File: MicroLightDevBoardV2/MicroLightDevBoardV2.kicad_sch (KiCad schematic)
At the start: 77 parts, among them J1 Conn_01x05_Socket, J10 Conn_01x02_Socket, J11 Conn_01x05_Socket, J12 Conn_01x02_Socket, J13 Conn_01x04_Socket, J14 Conn_01x04_Socket, J15 Conn_01x05_Socket, J16 Conn_01x01_Socket, J17 Conn_01x04_Socket, J18 Conn_01x02_Socket, J19 Conn_01x02_Socket, J2 Conn_01x05_Socket, J20 Conn_01x03_Socket, J21 Conn_01x03_Socket, J22 Conn_01x02_Socket, J23 Conn_01x02_Socket, J24 Conn_01x02_Socket, J25 Conn_01x02_Socket, J26 Conn_01x01_Socket, J27 Conn_01x06_Socket, J28 Conn_01x04_Socket, J29 Conn_01x04_Socket, J3 Conn_01x05_Socket, J30 Conn_01x04_Socket, J31 Conn_01x04_Socket, J32 Conn_01x04_Socket, J33 Conn_01x04_Socket, J34 Conn_01x04_Socket, J35 Conn_01x04_Socket, J36 Conn_01x04_Socket, J37 Conn_01x04_Socket, J38 Conn_01x04_Socket, J39 Conn_01x04_Socket, J4 Conn_01x05_Socket, J40 Conn_01x04_Socket, J41 Conn_01x04_Socket, J42 Conn_01x04_Socket, J43 Conn_01x04_Socket, J5 Conn_01x02_Socket, J6 Conn_01x02_Socket, J7 TYPE-C-31-M-12, J8 Conn_01x02_Socket, J9 Conn_01x02_Socket, U1 BQ25628RYKR, U2 ATtiny3226-M, U3 S-85S1AB33-I6T1U, U4 B3U-1000P, U5 B3U-1000P, U6 USBLC6-2P6, U7 MC3479

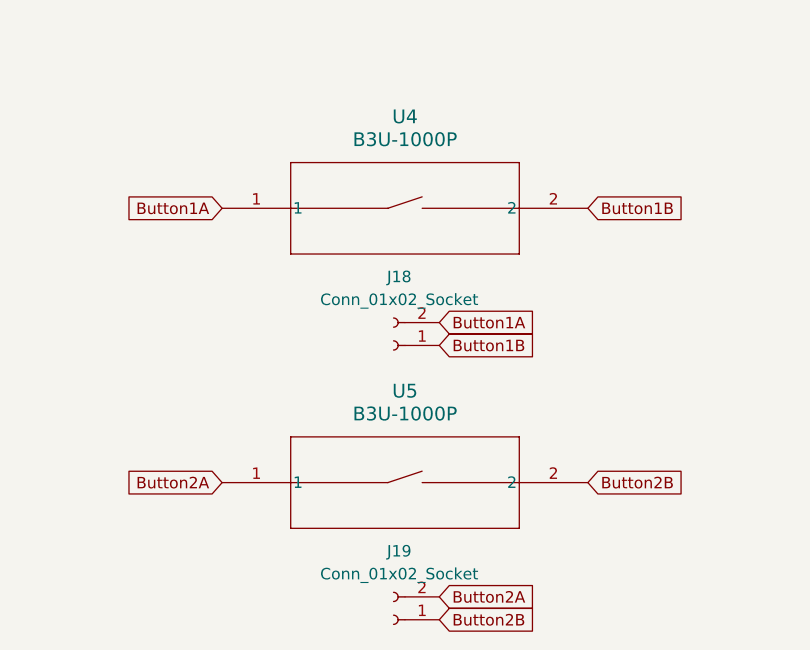
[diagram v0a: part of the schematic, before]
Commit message: add 1uh power inductor footprint from Wurth Elektronik
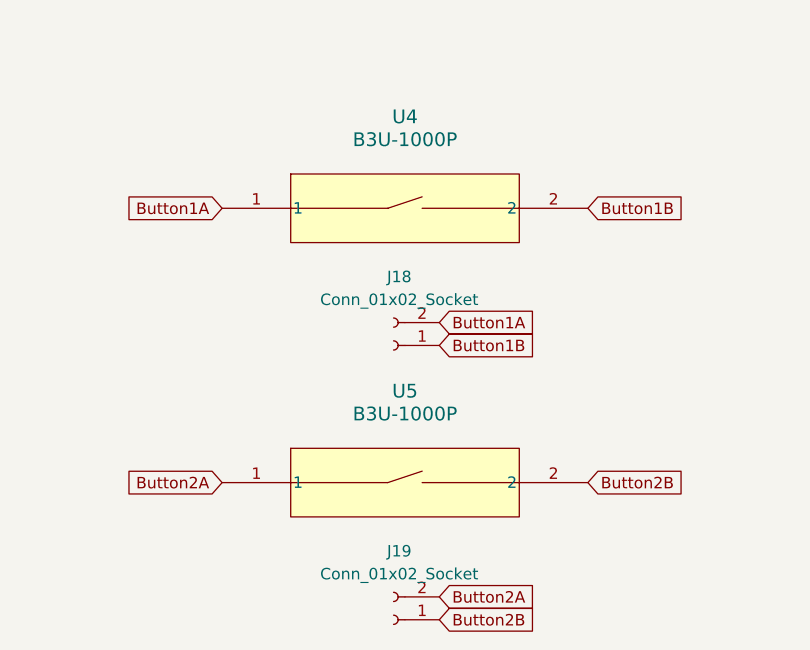
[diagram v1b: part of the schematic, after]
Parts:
- L2: footprint Inductor_SMD:L_0805_2012Metric -> MicroLightDevBoard:IND_2508-WE-MAPI_WRE; purchase (none) -> https://www.mouser.com/ProductDetail/Wurth-Elektronik/74438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
- U4, U5: footprint B3U-1000P -> MicroLightDevBoard:B3U-1000P
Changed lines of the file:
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@@
 			)
 		)
-		(property "Footprint" "Inductor_SMD:L_0805_2012Metric"
+		(property "Footprint" "MicroLightDevBoard:IND_2508-WE-MAPI_WRE"
 			(at 69.85 130.81 0)
 			(effects
@@
 			)
 		)
-		(property "Datasheet" "~"
+		(property "Datasheet" "https://www.we-online.com/components/products/datasheet/74438322010.pdf"
 			(at 69.85 130.81 0)
 			(effects
@@
 			)
 		)
+		(property "purchase" "https://www.mouser.com/ProductDetail/Wurth-Elektronik/74438322010?qs=ZB8tH5z5N7aonmcleKLsGw%3D%3D"
+			(at 69.85 130.81 90)
+			(effects
+				(font
+					(size 1.27 1.27)
+				)
+				(hide yes)
+			)
+		)
 		(pin "1"
 		)
@@
 	)
 	(symbol
+		(lib_name "B3U-1000P_1")
 		(lib_id "MicroLightDevBoard:B3U-1000P")
 		(at 185.42 175.26 0)
@@
 			)
 		)
-		(property "Footprint" "B3U-1000P"
+		(property "Footprint" "MicroLightDevBoard:B3U-1000P"
 			(at 185.42 175.26 0)
 			(effects
@@
 			)
 		)
-		(property "Footprint" "B3U-1000P"
+		(property "Footprint" "MicroLightDevBoard:B3U-1000P"
 			(at 185.42 205.74 0)
 			(effects

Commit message: added 2.2uh power inductor from wurth, updated first inductor footprint
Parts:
- L1: footprint Inductor_SMD:L_0805_2012Metric -> MicroLightDevBoard:74438343022_L; purchase (none) -> https://www.mouser.com/ProductDetail/Wurth-Elektronik/74438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
- L2: footprint MicroLightDevBoard:IND_2508-WE-MAPI_WRE -> MicroLightDevBoard:74438322010_L
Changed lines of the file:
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@@
 			)
 		)
-		(property "Footprint" "Inductor_SMD:L_0805_2012Metric"
+		(property "Footprint" "MicroLightDevBoard:74438343022_L"
 			(at 49.53 180.34 0)
 			(effects
@@
 			)
 		)
-		(property "Datasheet" "~"
+		(property "Datasheet" "https://www.we-online.com/components/products/datasheet/74438343022.pdf"
 			(at 49.53 180.34 0)
 			(effects
@@
 			)
 		)
-		(property "possible final version" ""
+		(property "purchase" "https://www.mouser.com/ProductDetail/Wurth-Elektronik/74438343022?qs=iC14BvcgY%2F123ryA6Z6D7g%3D%3D"
 			(at 49.53 180.34 90)
 			(effects
@@
 			)
 		)
-		(property "Footprint" "MicroLightDevBoard:IND_2508-WE-MAPI_WRE"
+		(property "Footprint" "MicroLightDevBoard:74438322010_L"
 			(at 69.85 130.81 0)
 			(effects

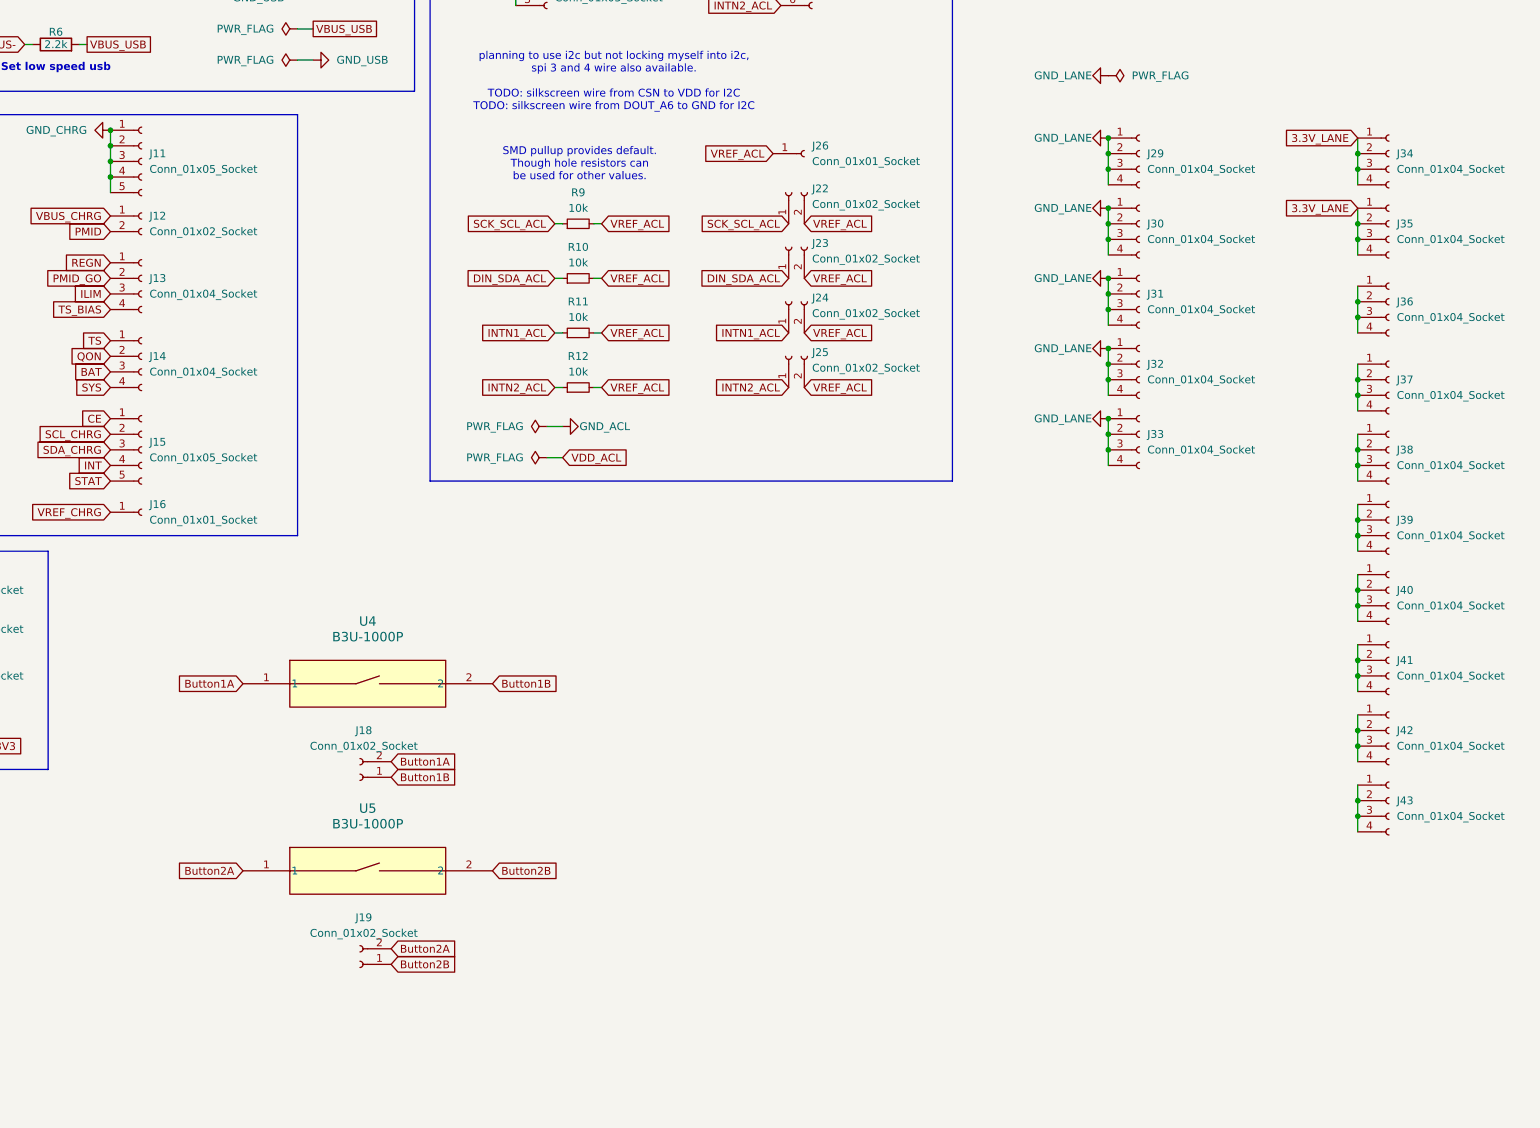
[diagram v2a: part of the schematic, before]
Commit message: adding lcsc part numbers, and more unconnected breakouts
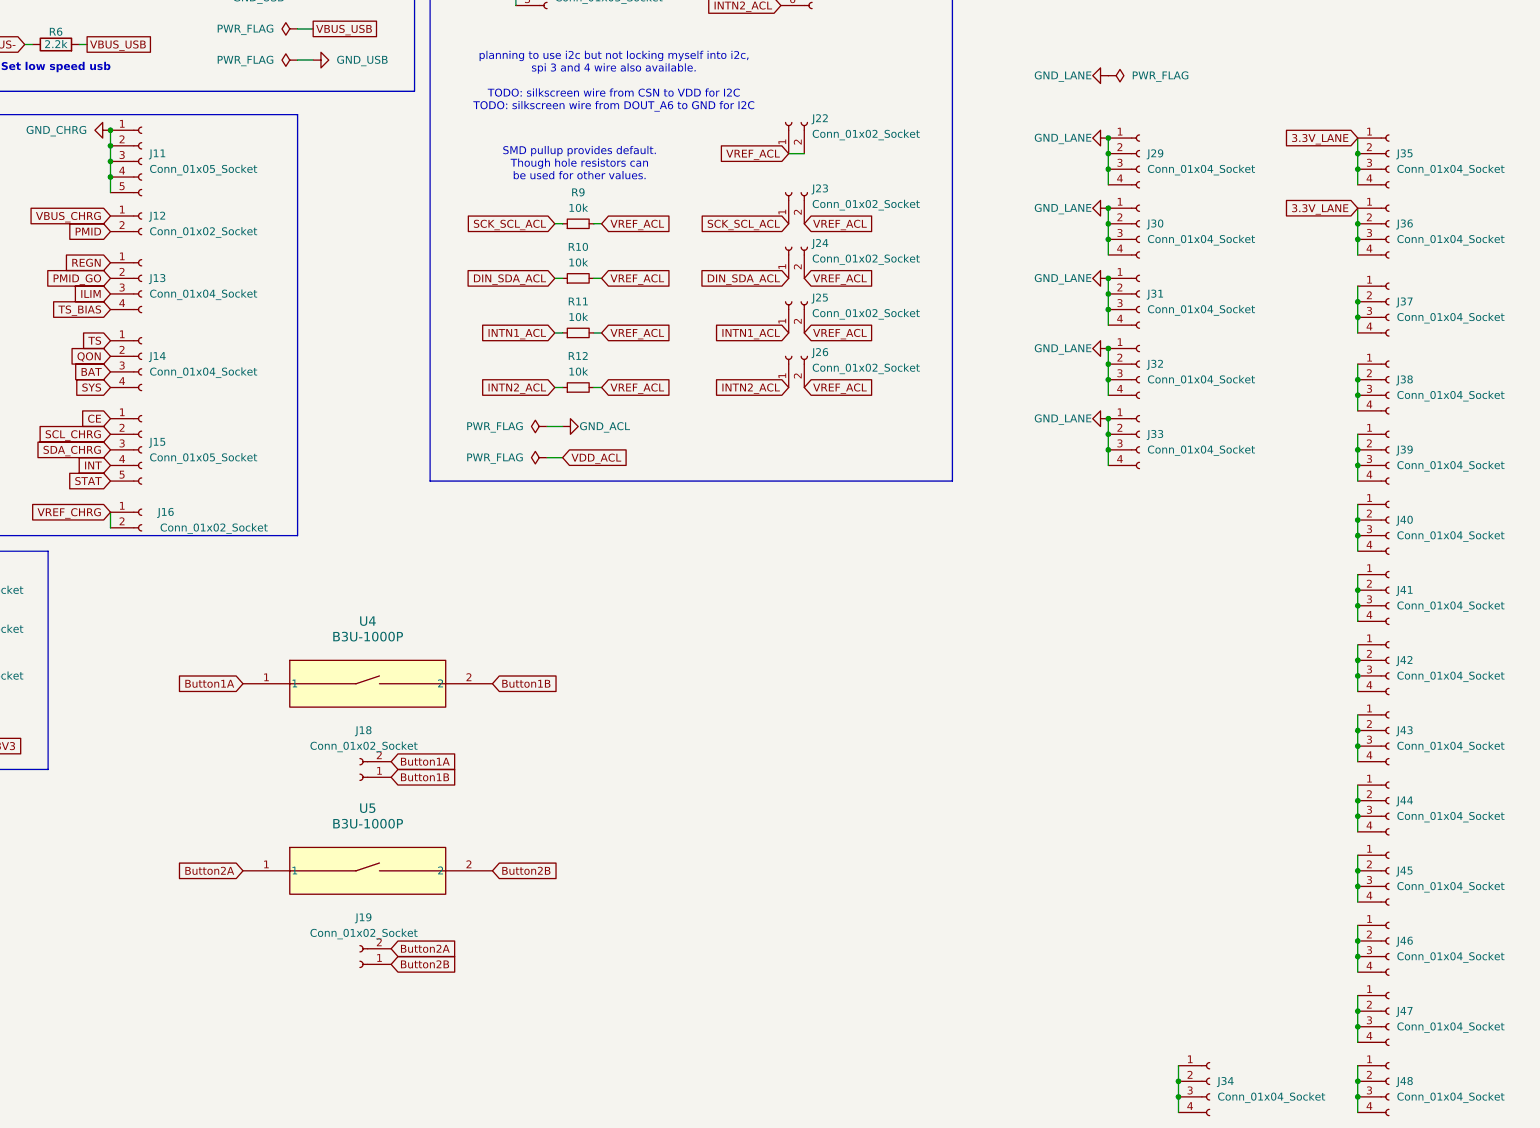
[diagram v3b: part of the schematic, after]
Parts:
- removed J16, J26: Conn_01x01_Socket, Connector_PinSocket_2.54mm:PinSocket_1x01_P2.54mm_Vertical, symbol Connector:Conn_01x01_Socket
- added J16, J22: Conn_01x02_Socket, Connector_PinSocket_2.54mm:PinSocket_1x02_P2.54mm_Vertical, symbol Connector:Conn_01x02_Socket
- added J34, J45, J46, J47, J48: Conn_01x04_Socket, Connector_PinSocket_2.54mm:PinSocket_1x04_P2.54mm_Vertical, symbol Connector:Conn_01x04_Socket
- renumbered J22 to J23, J23 to J24, J24 to J25, J25 to J26, J34 to J35, J35 to J36, J36 to J37, J37 to J38, J38 to J39, J39 to J40, J40 to J41, J41 to J42, J42 to J43, J43 to J44
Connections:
- net VREF_ACL: now also J22.1 (Pin_1), J22.2 (Pin_2)
- net VREF_CHRG: now also J16.1 (Pin_1), J16.2 (Pin_2)
- new net: J34.1 (Pin_1), J34.2 (Pin_2), J34.3 (Pin_3), J34.4 (Pin_4)
- new net: J47.1 (Pin_1), J47.2 (Pin_2), J47.3 (Pin_3), J47.4 (Pin_4)
- new net: J48.1 (Pin_1), J48.2 (Pin_2), J48.3 (Pin_3), J48.4 (Pin_4)
- new net: J46.1 (Pin_1), J46.2 (Pin_2), J46.3 (Pin_3), J46.4 (Pin_4)
- new net: J45.1 (Pin_1), J45.2 (Pin_2), J45.3 (Pin_3), J45.4 (Pin_4)

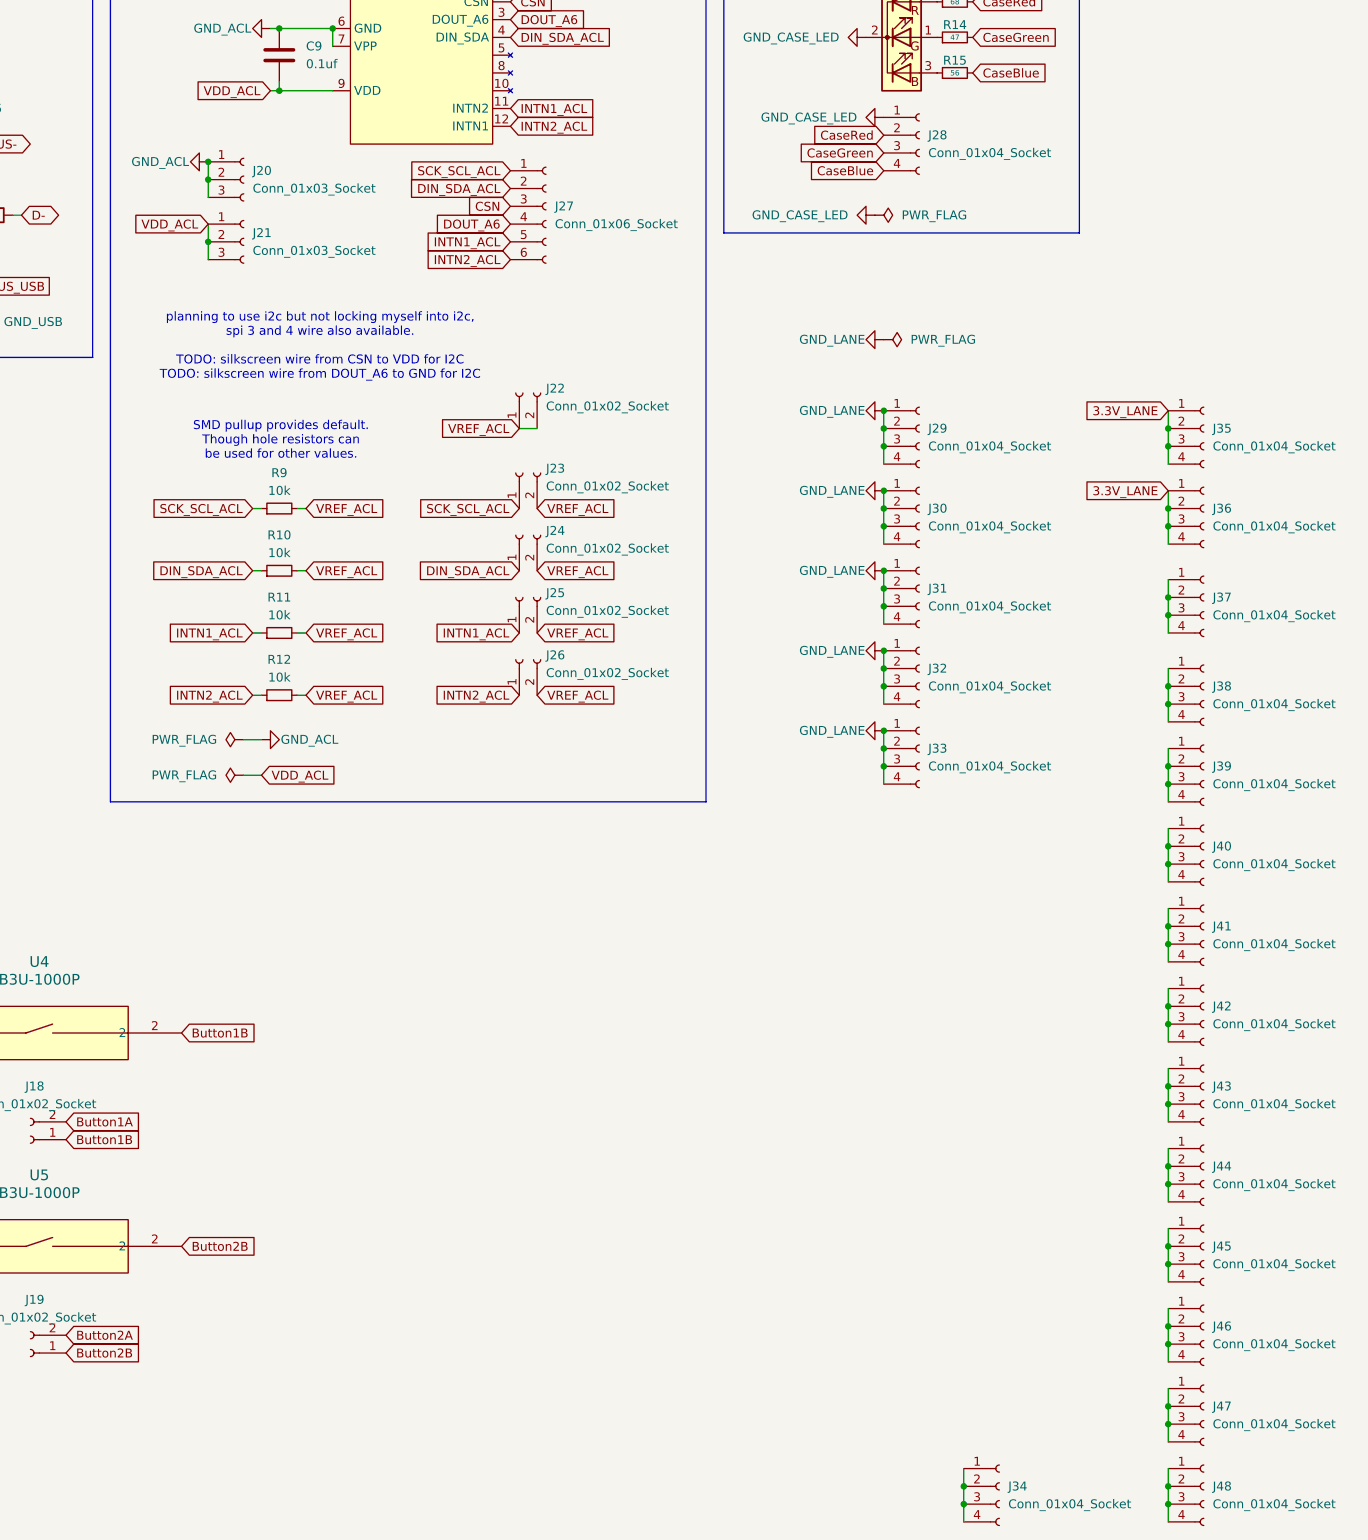
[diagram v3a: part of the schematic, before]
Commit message: cleaning up and adding connectors
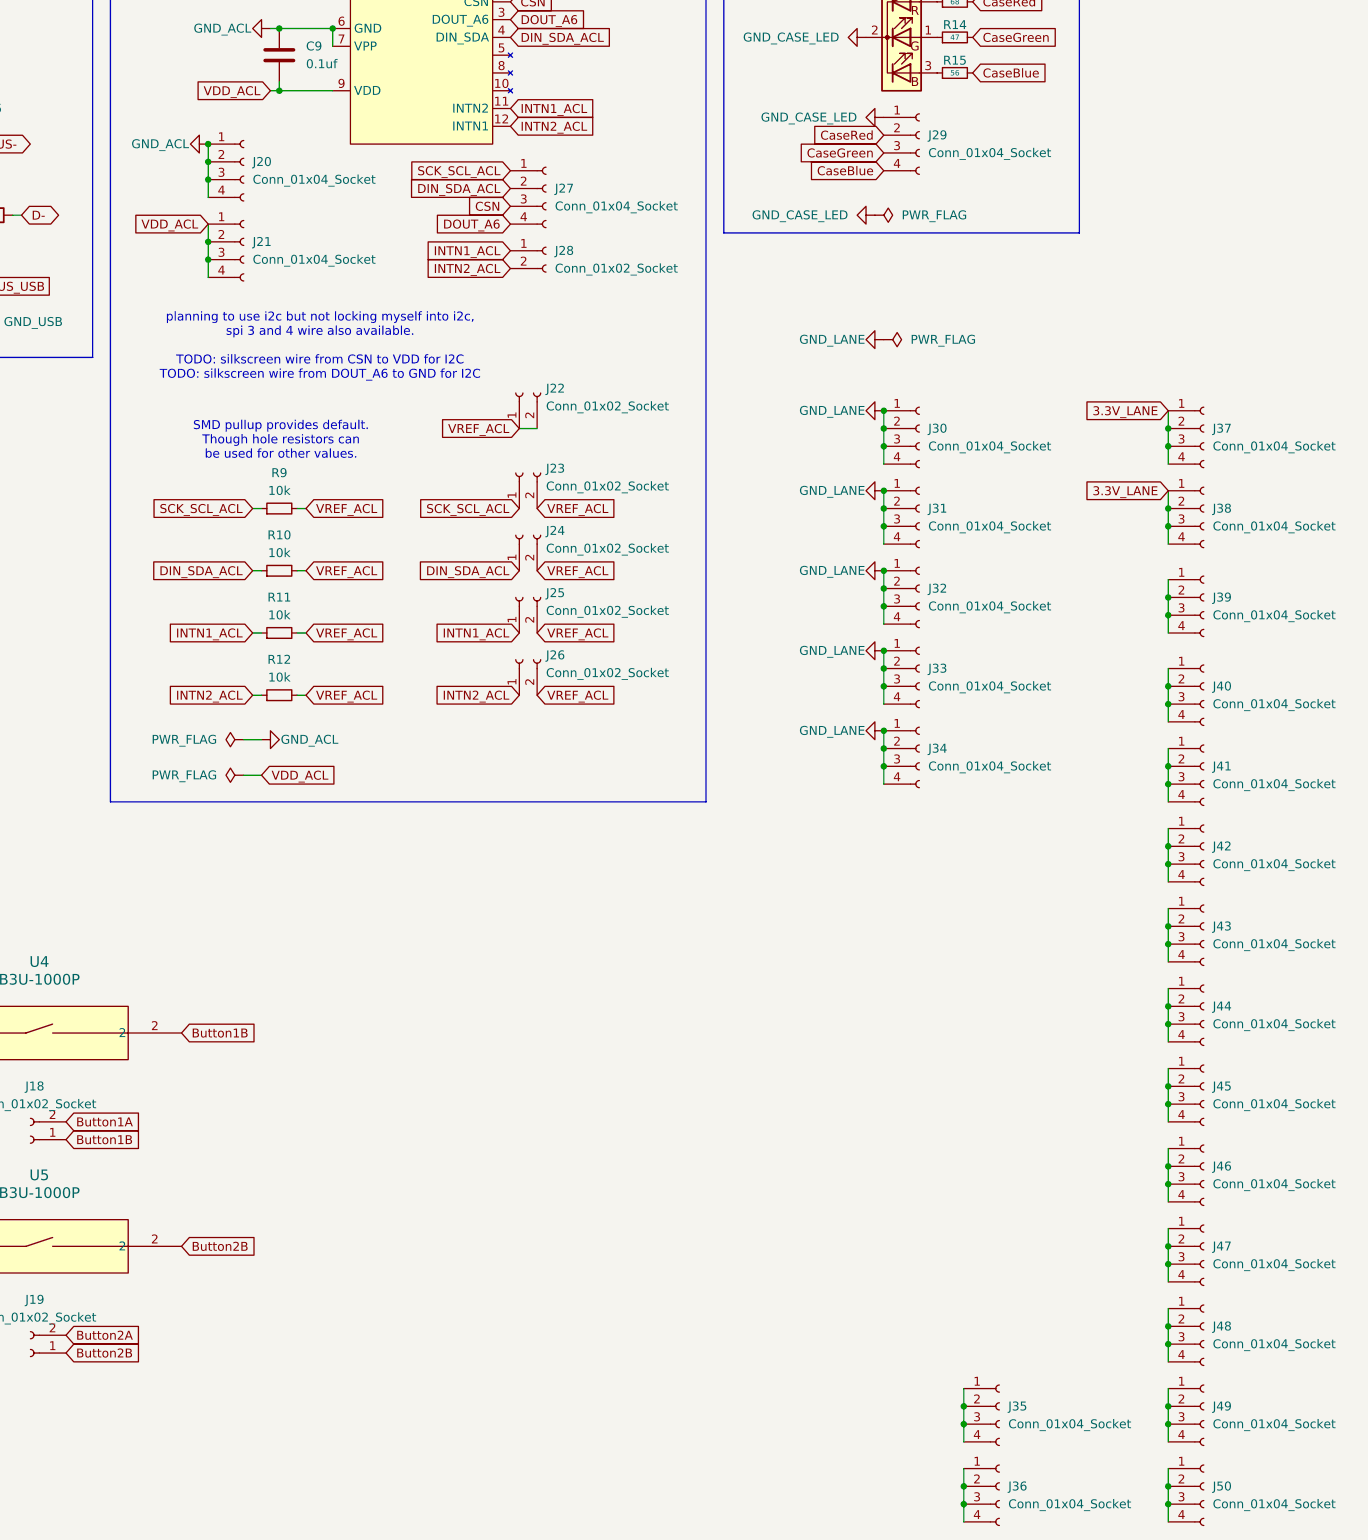
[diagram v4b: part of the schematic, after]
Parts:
- removed J20, J21: Conn_01x03_Socket, Connector_PinSocket_2.54mm:PinSocket_1x03_P2.54mm_Vertical, symbol Connector:Conn_01x03_Socket
- removed J27: Conn_01x06_Socket, Connector_PinSocket_2.54mm:PinSocket_1x06_P2.54mm_Vertical, symbol Connector:Conn_01x06_Socket
- added J20, J21, J27, J35: Conn_01x04_Socket, Connector_PinSocket_2.54mm:PinSocket_1x04_P2.54mm_Vertical, symbol Connector:Conn_01x04_Socket
- added J28: Conn_01x02_Socket, Connector_PinSocket_2.54mm:PinSocket_1x02_P2.54mm_Vertical, symbol Connector:Conn_01x02_Socket
- renumbered J28 to J29, J29 to J30, J30 to J31, J31 to J32, J32 to J33, J33 to J34, J34 to J36, J35 to J37, J36 to J38, J37 to J39, J38 to J40, J39 to J41, J40 to J42, J41 to J43, J42 to J44, J43 to J45, J44 to J46, J45 to J47, J46 to J48, J47 to J49, J48 to J50
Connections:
- net CSN: now also J27.3 (Pin_3)
- net DIN_SDA_ACL: now also J27.2 (Pin_2)
- net DOUT_A6: now also J27.4 (Pin_4)
- net GND_ACL: now also J20.1 (Pin_1), J20.2 (Pin_2), J20.3 (Pin_3), J20.4 (Pin_4)
- net INTN1_ACL: now also J28.1 (Pin_1)
- net INTN2_ACL: now also J28.2 (Pin_2)
- net SCK_SCL_ACL: now also J27.1 (Pin_1)
- net VDD_ACL: now also J21.1 (Pin_1), J21.2 (Pin_2), J21.3 (Pin_3), J21.4 (Pin_4)
- new net: J35.1 (Pin_1), J35.2 (Pin_2), J35.3 (Pin_3), J35.4 (Pin_4)
